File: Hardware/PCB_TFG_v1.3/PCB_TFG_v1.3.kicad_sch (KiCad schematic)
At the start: 47 parts, among them J2 Conn_01x06_Pin, J3 770669-1, Q1 8MHz, Q3 NPN, SW1 SW_Push, SW2 SW_Push, U1 STM32H523CET6, U2 TCAN330, U3 MCP1755ST-3302E/DB

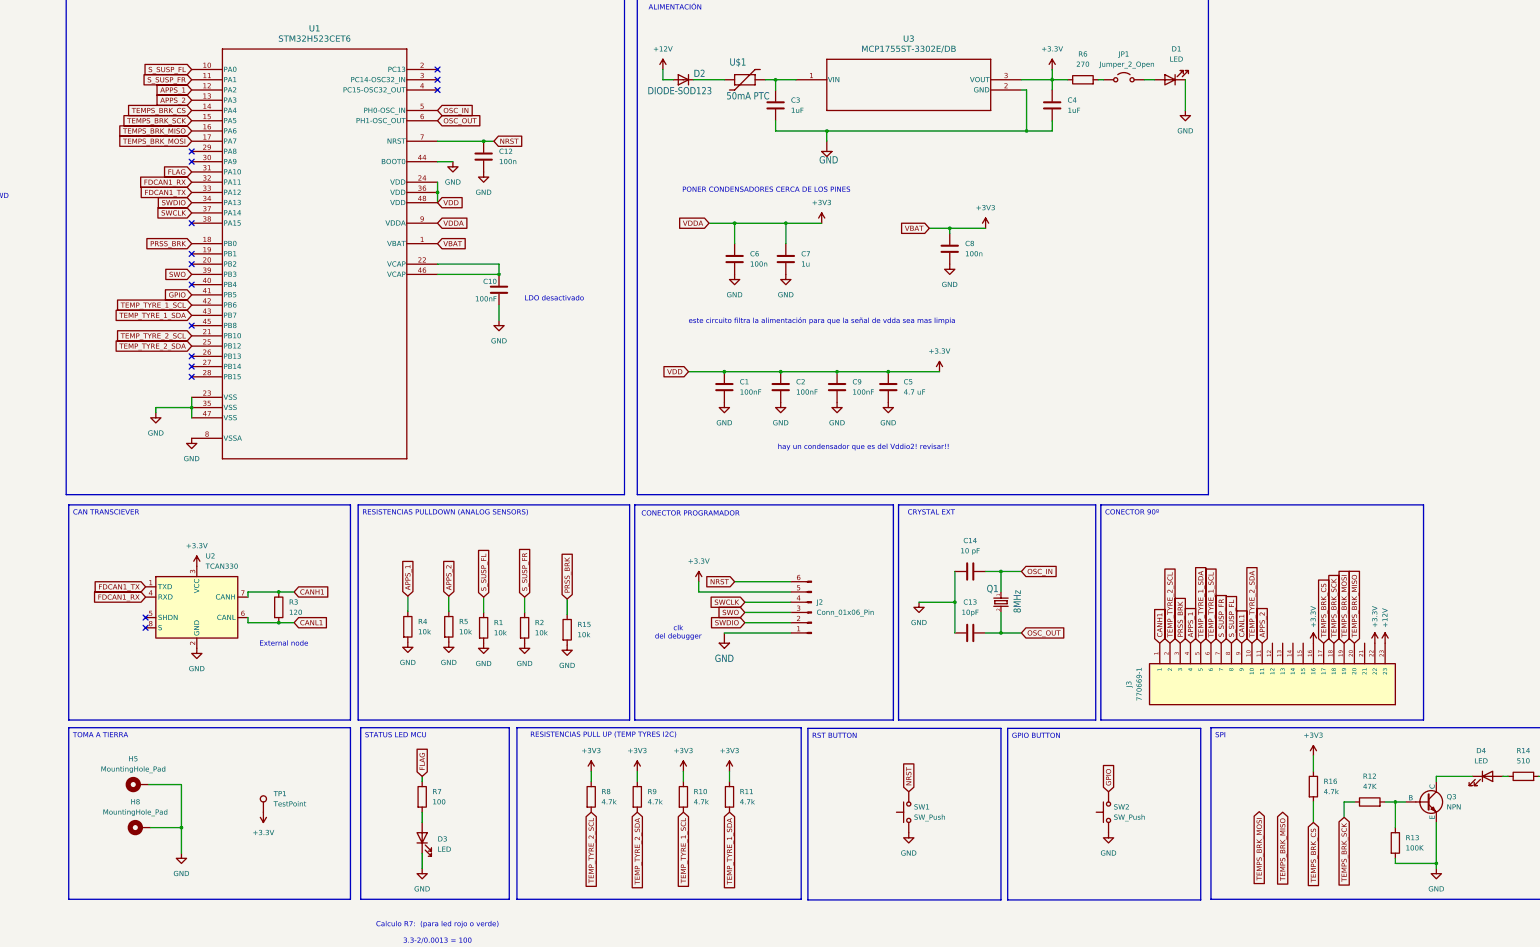
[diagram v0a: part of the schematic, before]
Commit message: MODIFICACIONES AL PCB
- Separación de Áreas Analógica y Digital.
- Creación de dos planos de GND y Vcc en capas intermedias.
- Recolocación de los C de desacoplo.
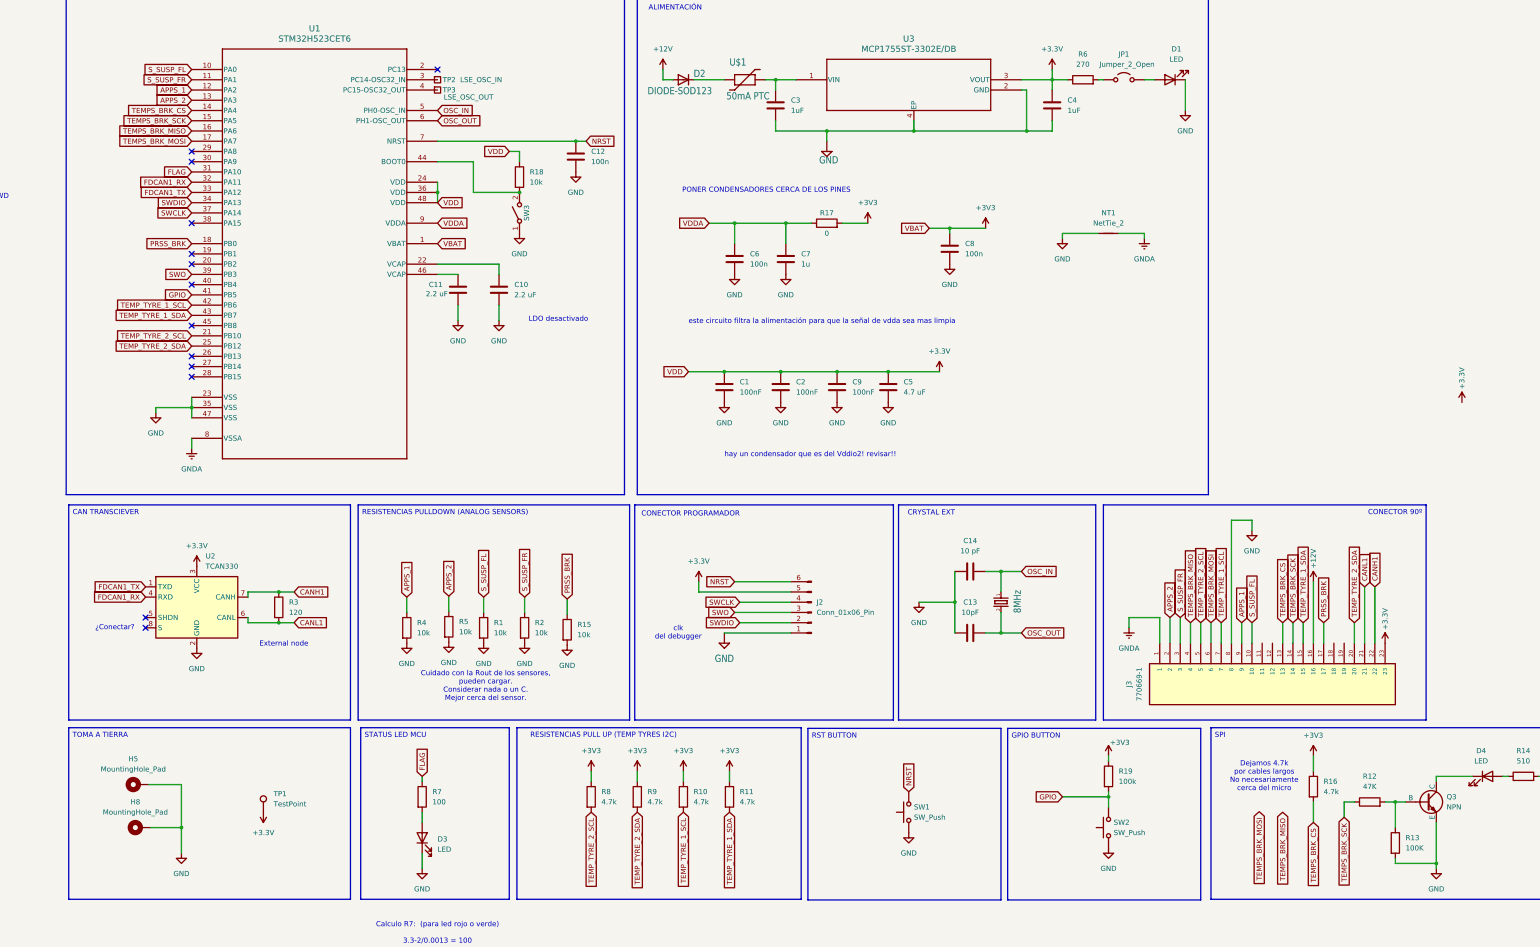
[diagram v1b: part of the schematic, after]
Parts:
- added C11: 2.2 uF, Capacitor_SMD:C_0805_2012Metric_Pad1.18x1.45mm_HandSolder, symbol Device:C
- added NT1: NetTie_2, NetTie:NetTie-2_SMD_Pad0.5mm, symbol Device:NetTie_2
- added R17: 0, Resistor_SMD:R_0805_2012Metric_Pad1.20x1.40mm_HandSolder, symbol Device:R
- added R18: 10k, Resistor_SMD:R_0805_2012Metric_Pad1.20x1.40mm_HandSolder, symbol Device:R
- added R19: 100k, Resistor_SMD:R_0805_2012Metric_Pad1.20x1.40mm_HandSolder, symbol Device:R
- added SW3: SW_SPST, symbol Switch:SW_SPST
- added TP2: LSE_OSC_IN, TestPoint:TestPoint_Pad_1.0x1.0mm, symbol Connector:TestPoint_Square
- added TP3: LSE_OSC_OUT, TestPoint:TestPoint_Pad_1.0x1.0mm, symbol Connector:TestPoint_Square
- C10: value 100nF -> 2.2 uF
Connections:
- net +12V: now also J3.16; no longer J3.23
- net +3.3V: now also J3.23, R18.1; no longer J3.16, J3.22
- net +3V3: now also R17.2, R19.1; no longer C6.2, C7.2, U1.9 (VDDA)
- net APPS_1: now also J3.9; no longer J3.4
- net APPS_2: now also J3.2; no longer J3.11
- net CANH1: now also J3.22; no longer J3.1
- net CANL1: now also J3.21; no longer J3.9
- net GND: now also J3.8, U3.4 (EP), C11.2, NT1.1, SW3.1 (A); no longer U1.44 (BOOT0), U1.8 (VSSA)
- net GPIO: now also R19.2
- net PRSS_BRK: now also J3.17; no longer J3.3
- net S_SUSP_FL: now also J3.10; no longer J3.8
- net S_SUSP_FR: now also J3.3; no longer J3.7
- net TEMPS_BRK_CS: now also J3.13; no longer J3.17
- net TEMPS_BRK_MISO: now also J3.4; no longer J3.20
- net TEMPS_BRK_MOSI: now also J3.6; no longer J3.19
- net TEMPS_BRK_SCK: now also J3.14; no longer J3.18
- net TEMP_TYRE_1_SCL: now also J3.7; no longer J3.6
- net TEMP_TYRE_1_SDA: now also J3.15; no longer J3.5
- net TEMP_TYRE_2_SCL: now also J3.5; no longer J3.2
- net TEMP_TYRE_2_SDA: now also J3.20; no longer J3.10
- net at C10.1, U1.22 (VCAP): no longer U1.46 (VCAP)
- net at U1.3 (PC14-OSC32_IN): now also TP2.1
- net at U1.4 (PC15-OSC32_OUT): now also TP3.1
- new net: R18.2, SW3.2 (B), U1.44 (BOOT0)
- new net: C11.1, U1.46 (VCAP)
- new net GNDA: J3.1, NT1.2, U1.8 (VSSA)
- new net VDDA: C6.2, C7.2, R17.1, U1.9 (VDDA)
- no-connect marks 15 -> 13
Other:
- note added: "Cuidado con la Rout de los sensores, pueden cargar. Considerar nada o un C. Mejor cerca del sensor."
- note added: "Dejamos 4.7k por cables largos No necesariamente cerca del micro"
- note added: "¿Conectar?"
- moved on the sheet: C12, SW2

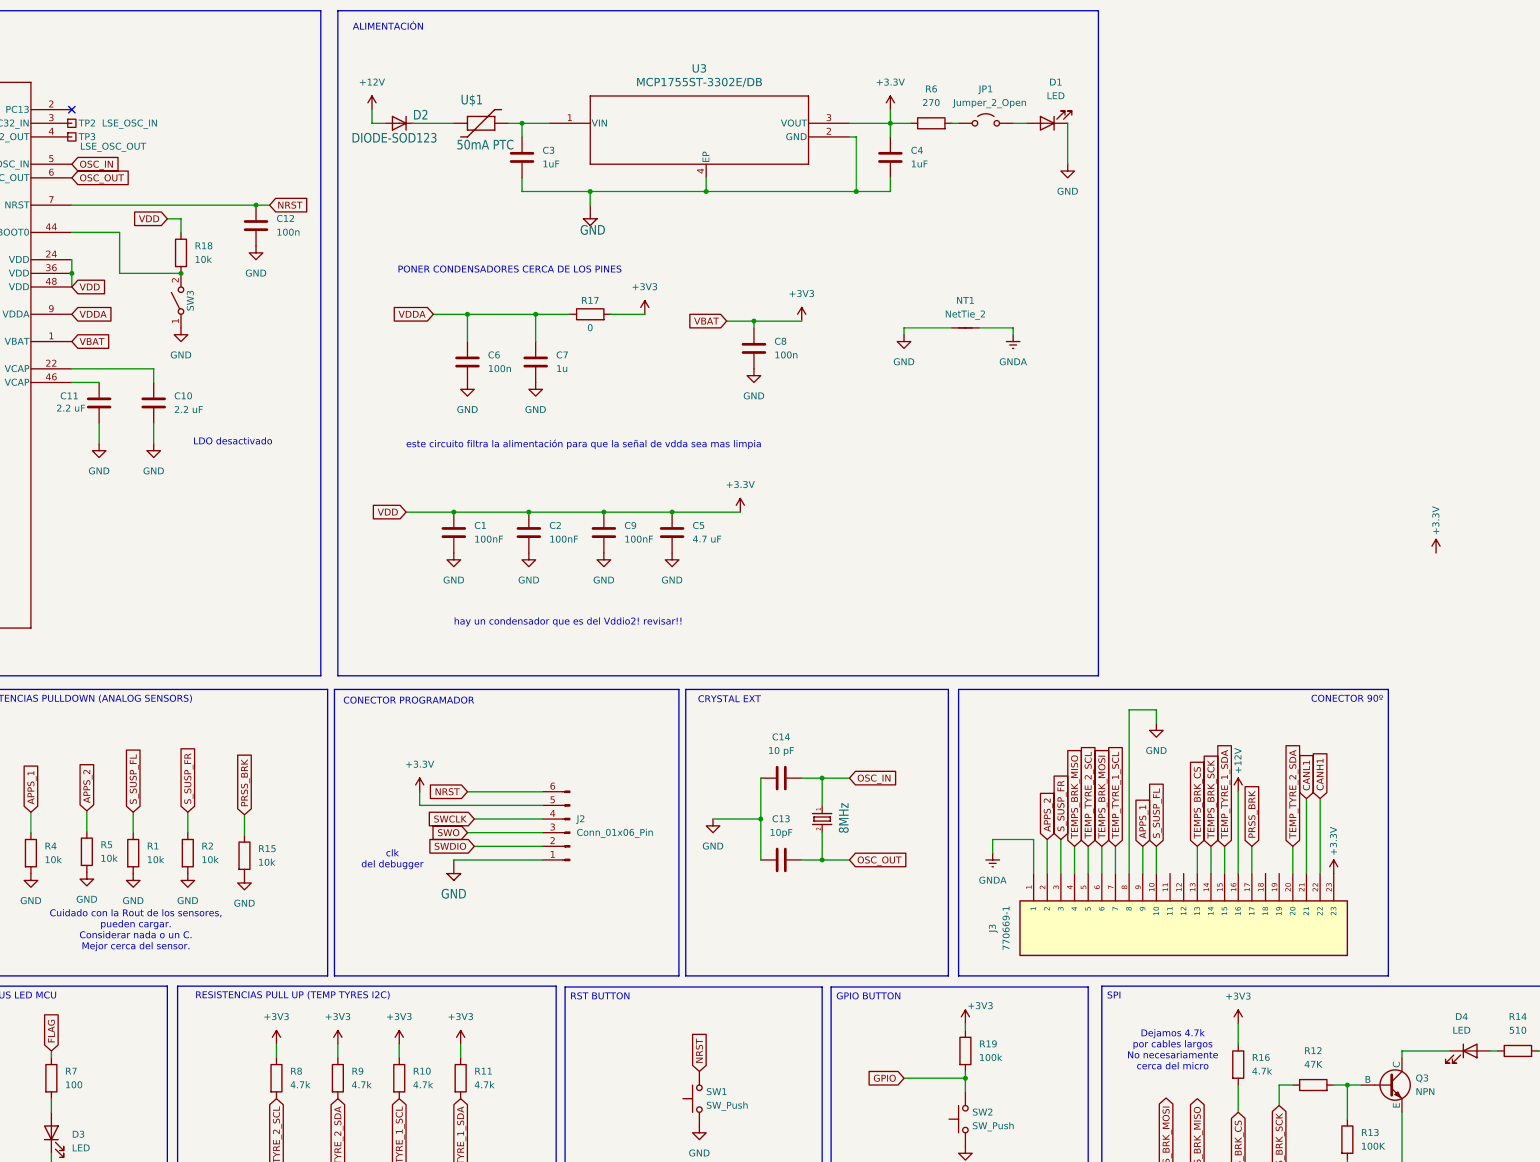
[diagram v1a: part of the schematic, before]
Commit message: ENRUTADO COMPLETADO
- Nueva versión del PCB ya enrutado.
- Modificadas huellas de algunos componentes, principalmente para incluir marca de posición.
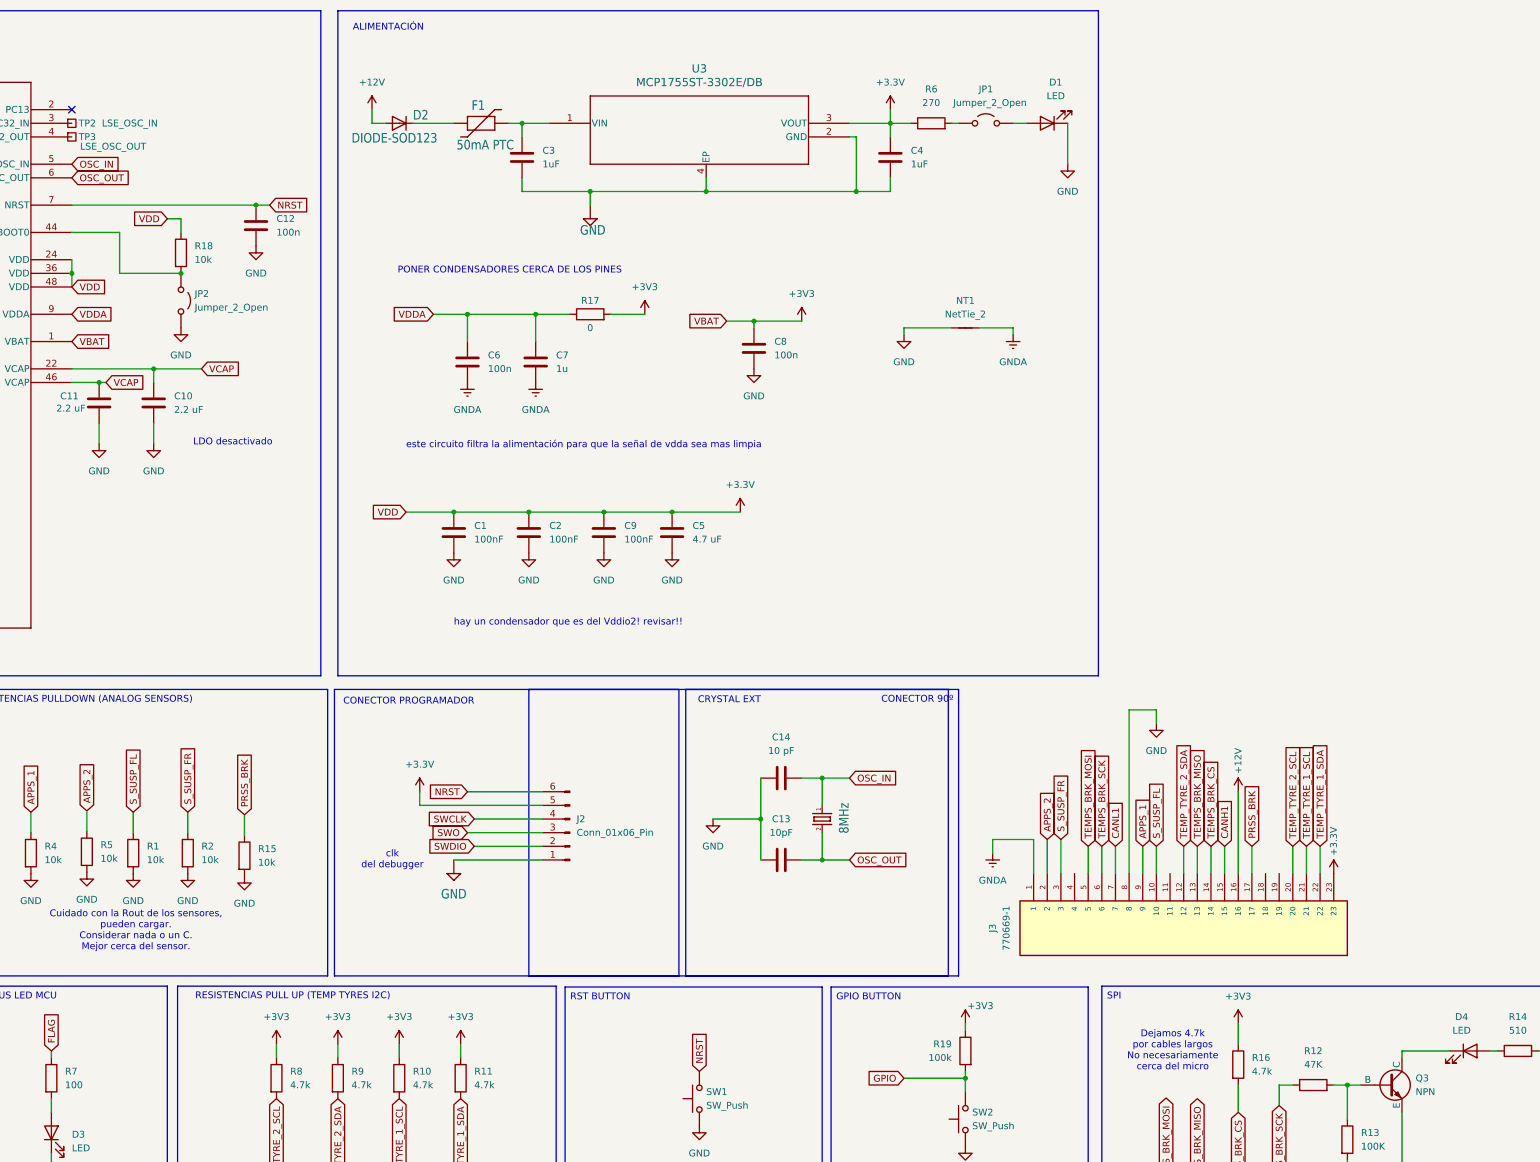
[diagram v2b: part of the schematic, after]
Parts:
- removed SW3: SW_SPST, symbol Switch:SW_SPST
- added JP2: Jumper_2_Open, Connector_PinHeader_2.54mm:PinHeader_1x02_P2.54mm_Vertical, symbol Jumper:Jumper_2_Open
- C12: footprint Capacitor_SMD:C_0603_1608Metric_Pad1.08x0.95mm_HandSolder -> Capacitor_SMD:C_0805_2012Metric_Pad1.18x1.45mm_HandSolder
- SW1, SW2: footprint Button_Switch_THT:SW_PUSH_6mm_H4.3mm -> Button_Switch_SMD:SW_SPST_B3U-1000P-B
- renumbered U$1 to F1
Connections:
- net CANH1: now also J3.15; no longer J3.22
- net CANL1: now also J3.7; no longer J3.21
- net GND: now also JP2.2 (B); no longer C6.1, C7.1
- net GNDA: now also C6.1, C7.1
- net TEMPS_BRK_CS: now also J3.14; no longer J3.13
- net TEMPS_BRK_MISO: now also J3.13; no longer J3.4
- net TEMPS_BRK_MOSI: now also J3.5; no longer J3.6
- net TEMPS_BRK_SCK: now also J3.6; no longer J3.14
- net TEMP_TYRE_1_SCL: now also J3.21; no longer J3.7
- net TEMP_TYRE_1_SDA: now also J3.22; no longer J3.15
- net TEMP_TYRE_2_SCL: now also J3.20; no longer J3.5
- net TEMP_TYRE_2_SDA: now also J3.12; no longer J3.20
- net at R18.2, U1.44 (BOOT0): now also JP2.1 (A)
- net VCAP: now reaches C10.1, U1.22 (VCAP)
- net VCAP: now also C11.1, U1.46 (VCAP)
